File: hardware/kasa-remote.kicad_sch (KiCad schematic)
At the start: 40 parts, among them J1 USB4105-GF-A, J2 S2B-PH-SM4-TB, J3 sh1106_vert, J4 sh1106_horiz, Q1 DMP2045U-7, SW1 RotaryEncoder_Switch, SW10 SW_Push, SW11 SW_Push, SW12 BOOT0, SW2 SW_Push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

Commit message: starting pcb work, might need to add more to the gitignore
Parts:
- added H1: MountingHole, symbol Mechanical:MountingHole
- added H2: MountingHole_Pad, symbol Mechanical:MountingHole_Pad
- C1, C2, C3, C4, C5, C6: footprint (none) -> Capacitor_SMD:C_0603_1608Metric
- D1: footprint (none) -> LED_SMD:LED_0603_1608Metric
- J3, J4: footprint (none) -> Connector_PinHeader_2.54mm:PinHeader_1x04_P2.54mm_Vertical
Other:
- note added: "Figure out which one to use"
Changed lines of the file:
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@@
+    (effects (font (size 1.27 1.27)) (justify left bottom))
+  )
+  (text "Figure out which one to use\n" (at 121.92 147.32 0)
     (effects (font (size 1.27 1.27)) (justify left bottom))
   )
@@
     )
   )
+  (symbol (lib_id "Mechanical:MountingHole_Pad") (at 135.89 139.7 0) (unit 1)
+    (in_bom yes) (on_board yes) (dnp no) (fields_autoplaced)
+    (property "Reference" "H2" (at 138.43 137.16 0)
+      (effects (font (size 1.27 1.27)) (justify left))
+    )
+    (property "Value" "MountingHole_Pad" (at 138.43 139.7 0)
+      (effects (font (size 1.27 1.27)) (justify left))
+    )
+    (property "Footprint" "" (at 135.89 139.7 0)
+      (effects (font (size 1.27 1.27)) hide)
+    )
+    (property "Datasheet" "~" (at 135.89 139.7 0)
+      (effects (font (size 1.27 1.27)) hide)
+    )
+    (pin "1")
+    (instances
+      (project "kasa-remote"
+        (path "/df7f32fc-d1fa-4117-93d4-056f22f352c5"
+          (reference "H2") (unit 1)
+        )
+      )
+    )
+  )
   (symbol (lib_id "power:GND") (at 95.885 173.99 0) (unit 1)
     (in_bom yes) (on_board yes) (dnp no) (fields_autoplaced)
@@
         (path "/df7f32fc-d1fa-4117-93d4-056f22f352c5"
           (reference "#PWR030") (unit 1)
+        )
+      )
+    )
+  )
+  (symbol (lib_id "Mechanical:MountingHole") (at 111.76 138.43 0) (unit 1)
+    (in_bom yes) (on_board yes) (dnp no) (fields_autoplaced)
+    (property "Reference" "H1" (at 114.3 137.16 0)
+      (effects (font (size 1.27 1.27)) (justify left))
+    )
+    (property "Value" "MountingHole" (at 114.3 139.7 0)
+      (effects (font (size 1.27 1.27)) (justify left))
+    )
+    (property "Footprint" "" (at 111.76 138.43 0)
+      (effects (font (size 1.27 1.27)) hide)
+    )
+    (property "Datasheet" "~" (at 111.76 138.43 0)
+      (effects (font (size 1.27 1.27)) hide)
+    )
+    (instances
+      (project "kasa-remote"
+        (path "/df7f32fc-d1fa-4117-93d4-056f22f352c5"
+          (reference "H1") (unit 1)
         )
       )
@@
       (effects (font (size 1.27 1.27)) (justify left))
     )
-    (property "Footprint" "" (at 260.985 42.545 0)
+    (property "Footprint" "Capacitor_SMD:C_0603_1608Metric" (at 260.985 42.545 0)
       (effects (font (size 1.27 1.27)) hide)
     )
@@
       (effects (font (size 1.27 1.27)) (justify left))
     )
-    (property "Footprint" "" (at 271.78 42.545 0)
+    (property "Footprint" "Capacitor_SMD:C_0603_1608Metric" (at 271.78 42.545 0)
       (effects (font (size 1.27 1.27)) hide)
     )
@@
       (effects (font (size 1.27 1.27)) (justify right))
     )
-    (property "Footprint" "" (at 220.345 127 0)
+    (property "Footprint" "Capacitor_SMD:C_0603_1608Metric" (at 220.345 127 0)
       (effects (font (size 1.27 1.27)) hide)
     )
@@
       (effects (font (size 1.27 1.27)) (justify left))
     )
-    (property "Footprint" "" (at 157.48 36.195 0)
+    (property "Footprint" "Connector_PinHeader_2.54mm:PinHeader_1x04_P2.54mm_Vertical" (at 157.48 36.195 0)
       (effects (font (size 1.27 1.27)) hide)
     )
@@
       (effects (font (size 1.27 1.27)))
     )
-    (property "Footprint" "" (at 222.885 85.09 0)
+    (property "Footprint" "LED_SMD:LED_0603_1608Metric" (at 222.885 85.09 0)
       (effects (font (size 1.27 1.27)) hide)
     )
@@
       (effects (font (size 1.27 1.27)))
     )
-    (property "Footprint" "" (at 274.32 78.105 0)
+    (property "Footprint" "Capacitor_SMD:C_0603_1608Metric" (at 274.32 78.105 0)
       (effects (font (size 1.27 1.27)) hide)
     )
@@
       (effects (font (size 1.27 1.27)) (justify left))
     )
-    (property "Footprint" "" (at 124.46 36.195 0)
+    (property "Footprint" "Connector_PinHeader_2.54mm:PinHeader_1x04_P2.54mm_Vertical" (at 124.46 36.195 0)
       (effects (font (size 1.27 1.27)) hide)
     )
@@
       (effects (font (size 1.27 1.27)) (justify left))
     )
-    (property "Footprint" "" (at 245.11 157.226 0)
+    (property "Footprint" "Capacitor_SMD:C_0603_1608Metric" (at 245.11 157.226 0)
       (effects (font (size 1.27 1.27)) hide)
     )
@@
       (effects (font (size 1.27 1.27)) (justify left))
     )
-    (property "Footprint" "" (at 219.075 44.45 0)
-      (effects (font (size 1.27 1.27)) hide)
-    )
+    (property "Footprint" "Capacitor_SMD:C_0603_1608Metric" (at 219.075 44.45 0)
+      (effects (font (size 1.27 1.27)) hide)
+    )

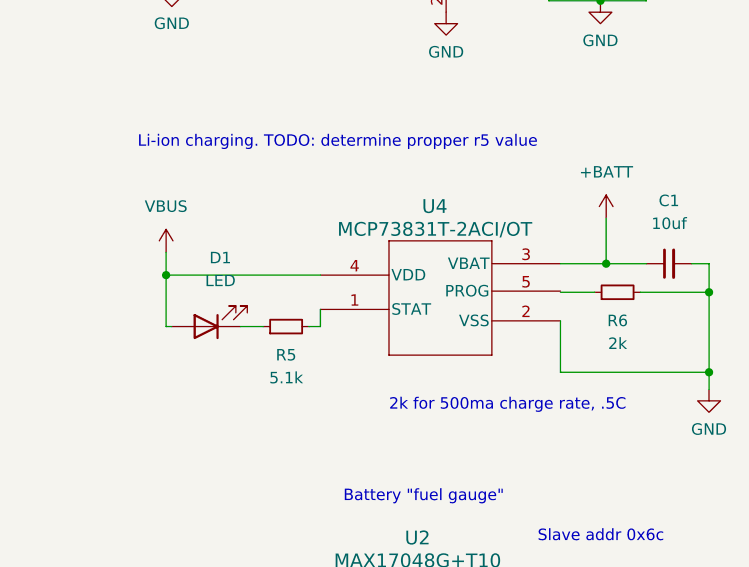
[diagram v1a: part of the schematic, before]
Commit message: fixed a couple mistakes in the schematic, organizing and starting layout
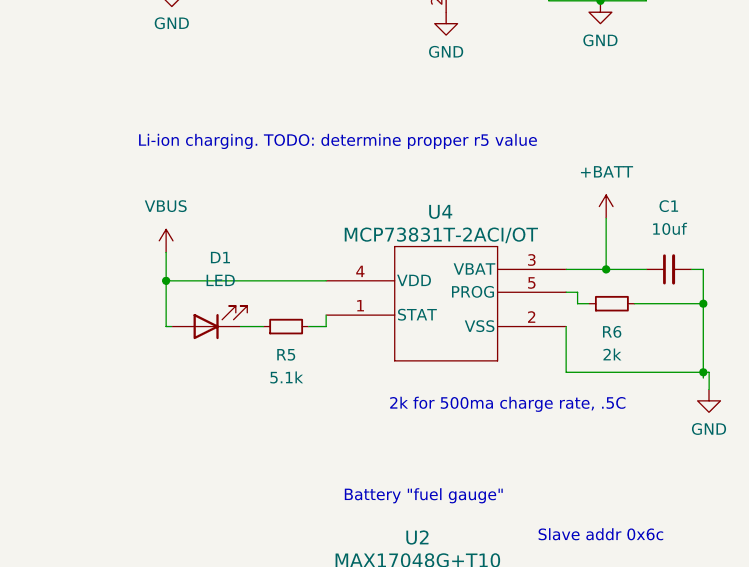
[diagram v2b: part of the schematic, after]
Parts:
- SW11: footprint Resistor_SMD:R_0603_1608Metric -> Button_Switch_SMD:SW_SPST_PTS810; mpn (none) -> PTS815 SJM 250 SMTR LFS
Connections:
- net at R6.1: now also U4.5 (PROG)
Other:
- moved on the sheet: C1, R6, U4
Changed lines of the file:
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@@
   (junction (at 220.345 122.555) (diameter 0) (color 0 0 0 0)
   )
+  (junction (at 278.13 90.17) (diameter 0) (color 0 0 0 0)
+  )
   (junction (at 224.79 129.54) (diameter 0) (color 0 0 0 0)
   )
@@
   (junction (at 78.74 39.37) (diameter 0) (color 0 0 0 0)
   )
-  (junction (at 218.44 79.375) (diameter 0) (color 0 0 0 0)
-  )
   (junction (at 271.78 40.005) (diameter 0) (color 0 0 0 0)
   )
@@
   (junction (at 192.405 34.925) (diameter 0) (color 0 0 0 0)
   )
-  (junction (at 278.765 81.28) (diameter 0) (color 0 0 0 0)
-  )
   (junction (at 65.405 99.06) (diameter 0) (color 0 0 0 0)
   )
@@
   (junction (at 128.905 175.26) (diameter 0) (color 0 0 0 0)
   )
+  (junction (at 278.13 82.55) (diameter 0) (color 0 0 0 0)
+  )
   (junction (at 65.405 114.3) (diameter 0) (color 0 0 0 0)
   )
+  (junction (at 218.44 80.01) (diameter 0) (color 0 0 0 0)
+  )
   (junction (at 65.405 106.68) (diameter 0) (color 0 0 0 0)
   )
@@
   (junction (at 213.36 40.005) (diameter 0) (color 0 0 0 0)
   )
-  (junction (at 267.335 78.105) (diameter 0) (color 0 0 0 0)
-  )
   (junction (at 220.345 120.015) (diameter 0) (color 0 0 0 0)
   )
@@
   (junction (at 236.22 40.005) (diameter 0) (color 0 0 0 0)
   )
+  (junction (at 267.335 78.74) (diameter 0) (color 0 0 0 0)
+  )
   (junction (at 266.7 48.895) (diameter 0) (color 0 0 0 0)
   )
-  (junction (at 278.765 90.17) (diameter 0) (color 0 0 0 0)
-  )
   (junction (at 200.025 34.925) (diameter 0) (color 0 0 0 0)
   )
@@
     (stroke (width 0) (type default))
   )
-  (wire (pts (xy 234.315 85.09) (xy 235.585 85.09))
+  (wire (pts (xy 264.16 82.55) (xy 265.43 82.55))
+    (stroke (width 0) (type default))
+  )
+  (wire (pts (xy 234.315 85.09) (xy 236.22 85.09))
     (stroke (width 0) (type default))
   )
@@
     (stroke (width 0) (type default))
   )
-  (wire (pts (xy 262.255 90.17) (xy 278.765 90.17))
-    (stroke (width 0) (type default))
-  )
   (wire (pts (xy 65.405 109.22) (xy 65.405 111.76))
     (stroke (width 0) (type default))
@@
     (stroke (width 0) (type default))
   )
-  (wire (pts (xy 218.44 85.09) (xy 218.44 79.375))
+  (wire (pts (xy 270.51 82.55) (xy 278.13 82.55))
+    (stroke (width 0) (type default))
+  )
+  (wire (pts (xy 218.44 85.09) (xy 218.44 80.01))
     (stroke (width 0) (type default))
   )
@@
     (stroke (width 0) (type default))
   )
-  (wire (pts (xy 235.585 85.09) (xy 235.585 83.185))
+  (wire (pts (xy 264.16 82.55) (xy 264.16 81.28))
+    (stroke (width 0) (type default))
+  )
+  (wire (pts (xy 236.22 85.09) (xy 236.22 83.82))
     (stroke (width 0) (type default))
   )
@@
     (stroke (width 0) (type default))
   )
-  (wire (pts (xy 267.335 78.105) (xy 271.78 78.105))
+  (wire (pts (xy 267.335 78.74) (xy 271.78 78.74))
+    (stroke (width 0) (type default))
+  )
+  (wire (pts (xy 278.13 90.17) (xy 278.765 90.17))
     (stroke (width 0) (type default))
   )
@@
     (stroke (width 0) (type default))
   )
-  (wire (pts (xy 262.255 81.28) (xy 266.065 81.28))
-    (stroke (width 0) (type default))
-  )
   (wire (pts (xy 213.36 40.005) (xy 219.075 40.005))
     (stroke (width 0) (type default))
   )
+  (wire (pts (xy 264.16 81.28) (xy 262.89 81.28))
+    (stroke (width 0) (type default))
+  )
   (wire (pts (xy 135.128 60.96) (xy 124.714 60.96))
     (stroke (width 0) (type default))
@@
     (stroke (width 0) (type default))
   )
+  (wire (pts (xy 262.89 90.17) (xy 278.13 90.17))
+    (stroke (width 0) (type default))
+  )
   (wire (pts (xy 78.74 39.37) (xy 83.185 39.37))
     (stroke (width 0) (type default))
@@
     (stroke (width 0) (type default))
   )
-  (wire (pts (xy 218.44 79.375) (xy 235.585 79.375))
-    (stroke (width 0) (type default))
-  )
-  (wire (pts (xy 262.255 84.455) (xy 262.255 90.17))
+  (wire (pts (xy 218.44 80.01) (xy 236.22 80.01))
+    (stroke (width 0) (type default))
+  )
+  (wire (pts (xy 262.89 85.09) (xy 262.89 90.17))
     (stroke (width 0) (type default))
   )
@@
     (stroke (width 0) (type default))
   )
-  (wire (pts (xy 278.765 81.28) (xy 278.765 90.17))
+  (wire (pts (xy 278.13 90.805) (xy 278.13 90.17))
     (stroke (width 0) (type default))
   )
@@
     (stroke (width 0) (type default))
   )
-  (wire (pts (xy 267.335 73.025) (xy 267.335 78.105))
+  (wire (pts (xy 267.335 73.025) (xy 267.335 78.74))
     (stroke (width 0) (type default))
   )
@@
     (stroke (width 0) (type default))
   )
-  (wire (pts (xy 278.765 78.105) (xy 278.765 81.28))
+  (wire (pts (xy 278.13 78.74) (xy 278.13 82.55))
     (stroke (width 0) (type default))
   )
@@
     (stroke (width 0) (type default))
   )
-  (wire (pts (xy 218.44 76.835) (xy 218.44 79.375))
-    (stroke (width 0) (type default))
-  )
-  (wire (pts (xy 276.86 78.105) (xy 278.765 78.105))
+  (wire (pts (xy 218.44 76.835) (xy 218.44 80.01))
+    (stroke (width 0) (type default))
+  )
+  (wire (pts (xy 276.86 78.74) (xy 278.13 78.74))
     (stroke (width 0) (type default))
   )
@@
     (stroke (width 0) (type default))
   )
+  (wire (pts (xy 278.13 82.55) (xy 278.13 90.17))
+    (stroke (width 0) (type default))
+  )
   (wire (pts (xy 224.79 129.54) (xy 224.79 131.445))
     (stroke (width 0) (type default))
@@
     (stroke (width 0) (type default))
   )
-  (wire (pts (xy 262.255 78.105) (xy 267.335 78.105))
+  (wire (pts (xy 262.89 78.74) (xy 267.335 78.74))
     (stroke (width 0) (type default))
   )
@@
   )
   (wire (pts (xy 245.11 153.162) (xy 245.11 154.686))
-    (stroke (width 0) (type default))
-  )
-  (wire (pts (xy 271.145 81.28) (xy 278.765 81.28))
     (stroke (width 0) (type default))
   )
@@
     )
   )
-  (symbol (lib_id "Device:R_Small") (at 268.605 81.28 90) (unit 1)
+  (symbol (lib_id "Device:R_Small") (at 267.97 82.55 90) (unit 1)
     (in_bom yes) (on_board yes) (dnp no)
-    (property "Reference" "R6" (at 268.605 84.455 90)
-      (effects (font (size 1.27 1.27)))
-    )
-    (property "Value" "2k" (at 268.605 86.995 90)
-      (effects (font (size 1.27 1.27)))
-    )
-    (property "Footprint" "Resistor_SMD:R_0603_1608Metric" (at 268.605 81.28 0)
-      (effects (font (size 1.27 1.27)) hide)
-    )
-    (property "Datasheet" "~" (at 268.605 81.28 0)
+    (property "Reference" "R6" (at 267.97 85.725 90)
+      (effects (font (size 1.27 1.27)))
+    )
+    (property "Value" "2k" (at 267.97 88.265 90)
+      (effects (font (size 1.27 1.27)))
+    )
+    (property "Footprint" "Resistor_SMD:R_0603_1608Metric" (at 267.97 82.55 0)
+      (effects (font (size 1.27 1.27)) hide)
+    )
+    (property "Datasheet" "~" (at 267.97 82.55 0)
       (effects (font (size 1.27 1.27)) hide)
     )
@@
     )
   )
-  (symbol (lib_id "Device:C_Small") (at 274.32 78.105 90) (unit 1)
-    (in_bom yes) (on_board yes) (dnp no) (fields_autoplaced)
-    (property "Reference" "C1" (at 274.3263 71.12 90)
-      (effects (font (size 1.27 1.27)))
-    )
-    (property "Value" "10uf" (at 274.3263 73.66 90)
-      (effects (font (size 1.27 1.27)))
-    )
-    (property "Footprint" "Capacitor_SMD:C_0603_1608Metric" (at 274.32 78.105 0)
-      (effects (font (size 1.27 1.27)) hide)
-    )
-    (property "Datasheet" "~" (at 274.32 78.105 0)
+  (symbol (lib_id "Device:C_Small") (at 274.32 78.74 90) (unit 1)
+    (in_bom yes) (on_board yes) (dnp no) (fields_autoplaced)
+    (property "Reference" "C1" (at 274.3263 71.755 90)
+      (effects (font (size 1.27 1.27)))
+    )
+    (property "Value" "10uf" (at 274.3263 74.295 90)
+      (effects (font (size 1.27 1.27)))
+    )
+    (property "Footprint" "Capacitor_SMD:C_0603_1608Metric" (at 274.32 78.74 0)
+      (effects (font (size 1.27 1.27)) hide)
+    )
+    (property "Datasheet" "~" (at 274.32 78.74 0)
       (effects (font (size 1.27 1.27)) hide)
     )
@@
     )
   )
-  (symbol (lib_id "MCP7381:MCP73831T-2ACI_OT") (at 201.295 80.645 0) (unit 1)
-    (in_bom yes) (on_board yes) (dnp no) (fields_autoplaced)
-    (property "Reference" "U4" (at 248.285 71.755 0)
+  (symbol (lib_id "MCP7381:MCP73831T-2ACI_OT") (at 201.93 81.28 0) (unit 1)
+    (in_bom yes) (on_board yes) (dnp no) (fields_autoplaced)
+    (property "Reference" "U4" (at 248.92 72.39 0)
       (effects (font (size 1.524 1.524)))
     )
-    (property "Value" "MCP73831T-2ACI/OT" (at 248.285 74.295 0)
+    (property "Value" "MCP73831T-2ACI/OT" (at 248.92 74.93 0)
       (effects (font (size 1.524 1.524)))
     )
-    (property "Footprint" "MCP7381:SOT-23-5_MC_MCH" (at 248.285 92.583 0)
+    (property "Footprint" "MCP7381:SOT-23-5_MC_MCH" (at 248.92 93.218 0)
       (effects (font (size 1.27 1.27) italic) hide)
     )
-    (property "Datasheet" "MCP73831T-2ACI/OT" (at 248.285 90.297 0)
+    (property "Datasheet" "MCP73831T-2ACI/OT" (at 248.92 90.932 0)
       (effects (font (size 1.27 1.27) italic) hide)
     )
@@
       (effects (font (size 1.27 1.27)))
     )
-    (property "Footprint" "Resistor_SMD:R_0603_1608Metric" (at 260.35 148.082 0)
+    (property "Footprint" "Button_Switch_SMD:SW_SPST_PTS810" (at 260.35 148.082 0)
       (effects (font (size 1.27 1.27)) hide)
     )
@@
       (effects (font (size 1.27 1.27)) hide)
     )
+    (property "mpn" "PTS815 SJM 250 SMTR LFS" (at 260.35 153.162 0)
+      (effects (font (size 1.27 1.27)) hide)
+    )
+    (property "Mfg Part #" "" (at 260.35 153.162 0)
+      (effects (font (size 1.27 1.27)) hide)
+    )
